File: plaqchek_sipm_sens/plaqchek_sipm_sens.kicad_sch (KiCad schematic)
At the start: 36 parts, among them J1 Conn_01x04, U14 MIC5504-1.8YM5, U16 LDK320AM-R

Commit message: finish schematic
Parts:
- removed C11, C16, C22: 0.1uF, symbol Device:C_Small
- removed C3, C37: 1nF, symbol Device:C_Small
- removed C43, C44: 1uF, symbol Device:C_Small
- removed C45, C46: 10nF, symbol Device:C_Small
- removed D1: D_SiPM, symbol Device:D_SiPM
- removed R1: 7k, symbol Device:R_Small_US
- removed R11: 10k, symbol Device:R_Small_US
- removed R12, R14: 0, symbol Device:R_Small_US
- removed R20: 22R, symbol Device:R_Small_US
- removed R35, R36: 50R, symbol Device:R_Small_US
- removed U13: ~, symbol plaqchek_mlb:MCP1501T-50E
- removed U16: LDK320AM-R, symbol plaqchek_mlb:LDK320AM-R
- removed U2, U4, U9: ~, symbol plaqchek_mlb:OPA814
- removed U5: ~, symbol plaqchek_mlb:MCP33131-10-E/MS
- added C19, C28, C29, C31, C9: 1uF, symbol Device:C_Small
- added C26: 0.33uF, symbol Device:C_Small
- added H1, H2, H3, H4: MountingHole_Pad, symbol Mechanical:MountingHole_Pad
- added J3: Conn_01x05, symbol Connector_Generic:Conn_01x05
- added R1 (x3), R15, R16, R17: 0, symbol Device:R_Small_US
- added R1 (x4): 0R, symbol Device:R_Small_US
- added R10: 350kR, symbol Device:R_Small_US
- added TP1, TP10, TP2, TP3, TP4, TP6, TP8, TP9: TestPoint, symbol Connector:TestPoint
- added TP10: -5VA, symbol Connector:TestPoint
- added TP9: 5VA, symbol Connector:TestPoint
- added U10: LDK320AM-R, symbol plaqchek_mlb:LDK320AM-R
- added U5: TPS7A2050PDBVR, symbol plaqchek:TPS7A2050PDBVR
- added U8: MC79M05_TO252, Package_TO_SOT_SMD:TO-252-2, symbol Regulator_Linear:MC79M05_TO252
- added U8: RT9072BGB, symbol plaqchek:RT9072BGB
- C10: value 0.1uF -> 1uF
- C17: value 1.7nF -> 0.18uF
- C18: value 10uF -> 1uF
- C20: value 0.1uF -> 2.2uF
- C21: value 0.1uF -> 1nF
- R13: value 10k -> 0R; now fitted
- R19: value 0 -> 100kR; now fitted
- R29: value 350kR -> 2.3kR
- R30: value 100kR -> 80kR
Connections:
- net SIPM_44V is gone; now on net SPI_3V3_ADC_CS: J1.1 (Pin_1)
- net VREF_ADC is gone; now on net SIPM_BIAS_OUT: C18.1
- net +1V8: now also R1.1, TP4.1; no longer C21.1, C38.1, U14.5 (VOUT)
- net +3V3: now also R13.2, J3.3 (Pin_3), TP9.1; no longer J1.3 (Pin_3), U14.3 (EN)
- net +5.35V: now also C29.1, R10.1, U10.5 (OUT); no longer C10.2, C20.1, R29.1
- net +6V: now also C28.1, C9.1, J3.2 (Pin_2), R17.2, U10.1 (IN), U10.3 (EN), U5.1 (IN); no longer J1.2 (Pin_2)
- net GND: now also C10.2, R19.2, C19.2, C26.1, C28.2, C29.2, C31.1, C9.2, J3.5 (Pin_5), R1.1, R1.2, R1.2, R1.2, R1.2, U10.2 (GND), U5.2 (GND), U8.1 (GND), U8.2 (SHDN); no longer C10.1, C21.2, R13.1
- net SPI_3V3_ADC_MISO: now also J1.2 (Pin_2)
- net SPI_3V3_ADC_SCLK: now also J1.3 (Pin_3)
- net at R29.2, R30.1: now also C21.2, U8.4 (FB)
- net at R19.1: now also R10.2, U10.4 (ADJ)
- net AIN_FILT renamed SIPM_BIAS_OUT
- net SIPM_BIAS_OUT: now also J3.1 (Pin_1), TP8.1, U8.1 (VIN)
- new net: C10.1, R15.2, TP9.1, U5.5 (OUT)
- new net: C19.1, C20.1, C21.1, R1.2, R29.1, TP2.1, U8.5 (VOUT)
- new net: C38.1, R1.2, TP3.1, U14.5 (VOUT)
- new net: H4.1, R1.1
- new net: C31.2, R16.2, TP10.1, U8.3 (VO)
- new net: H2.1, R1.1
- new net: H1.1, R1.1
- new net: R1.2, U8.2 (SHDN)
- new net: R17.1, U5.3 (EN)
- new net: R13.1, U14.3 (EN)
- new net: H3.1, R1.1
- new net +5VA: R15.1, TP6.1
- new net -5VA: R16.1, TP10.1
- new net -6V5: C26.2, J3.4 (Pin_4), U8.2 (VI)
- new net PD_BIAS: R1.1, TP1.1
- no-connect marks 0 -> 1
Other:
- added sheet SIPM Readout (plaqchek_sipm_read.kicad_sch)
- note added: "Max dropout V = 1.1V"
- note added: "Max dropout V = 145mV"
- note added: "R2 = R1 / (VOUT / 1.25V - 1) R1 must be below 100k Compensation capacitance = 25µs/R1"
- note removed: "Antialiasing Filter"
- note removed: "Buffer GBW = 250MHz"
- note removed: "C_in = 2.5pF, C_SiPM = 580pF, GBW = 250MHz Cf > 333 pF Choose Cf = 1nF"
- note removed: "Cf > (C_in + C_SiPM) / (Rf*GBW))"
- note removed: "Iout = 20mA"
- note removed: "Max 60Mhz"
- note removed: "Optional 2nd stage"
- note removed: "PDE = 62% at 420nm 12V Vov Gain = 7.2*10^6 Estimate 10^11 photons Thus Imax = (1.6*10^-16 C / photon) * (10^9 photons) * 0.62 * 7.2*10^6 = 0.00071424 A For Vswing = 5V: R = 2.5/0.00071424 = 7k ohms For 10^7 photons: V = 0.05V"
- note removed: "Place R14, R12 close to output of U9 R19 close to U2"
- note removed: "TIA - 1st stage"
- note removed: "Vin range: 5.2V to 5.5V Vout = 5V"
- note removed: "breakdown coltage = 32.5V typ 32V-33V Target Vov of around 12V Max Vov = 16V Min Vov = 5V Targed vbias = 44.5V max vbias = 48.5V min vbias = 37.5V"
- note removed: "cutoff freq = 2MHz"
- moved on the sheet: C36, C38, U14

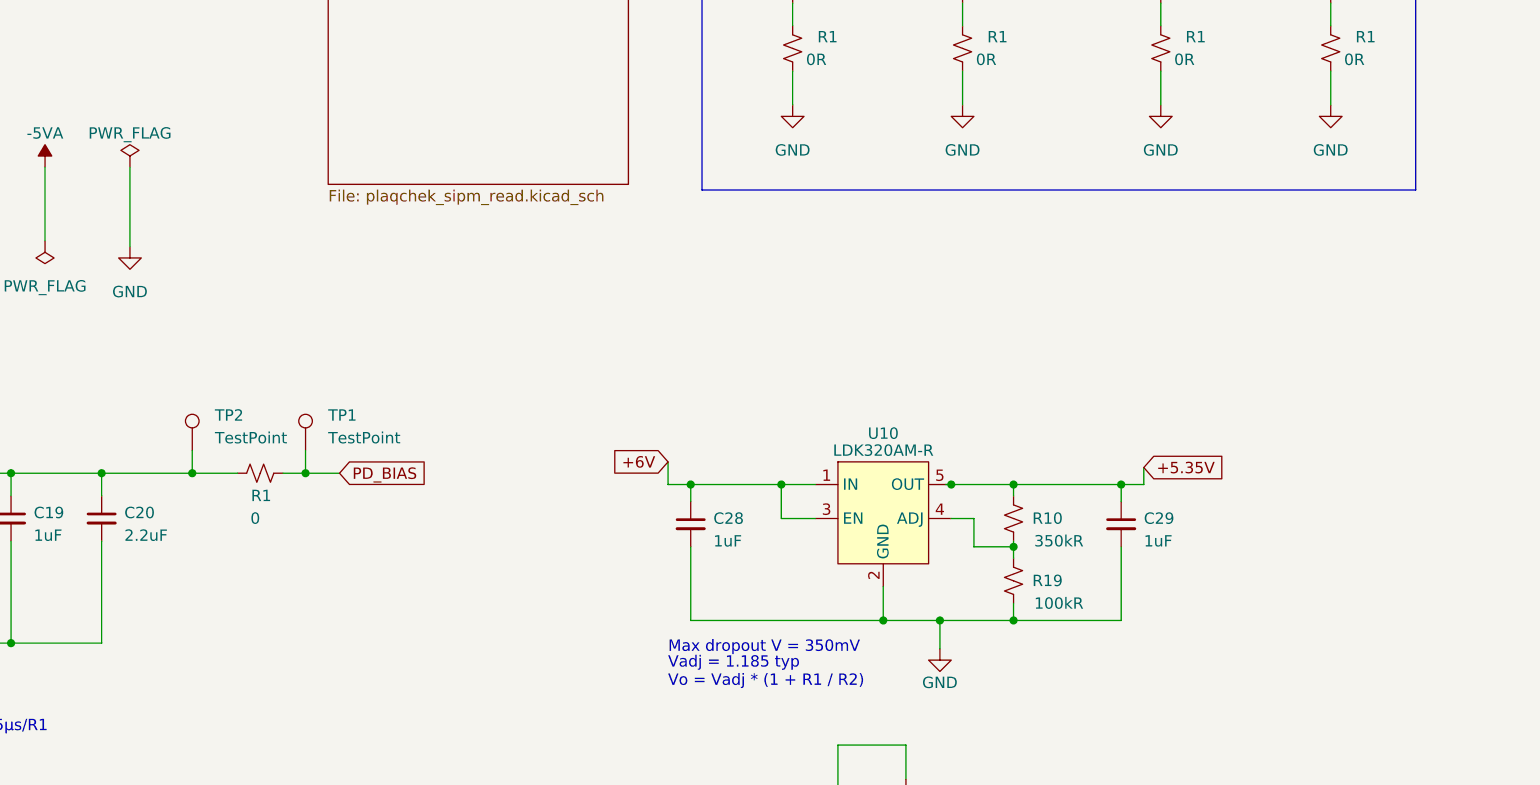
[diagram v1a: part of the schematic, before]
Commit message: modify TIA feedback cap value for new op amp, assign some footprints
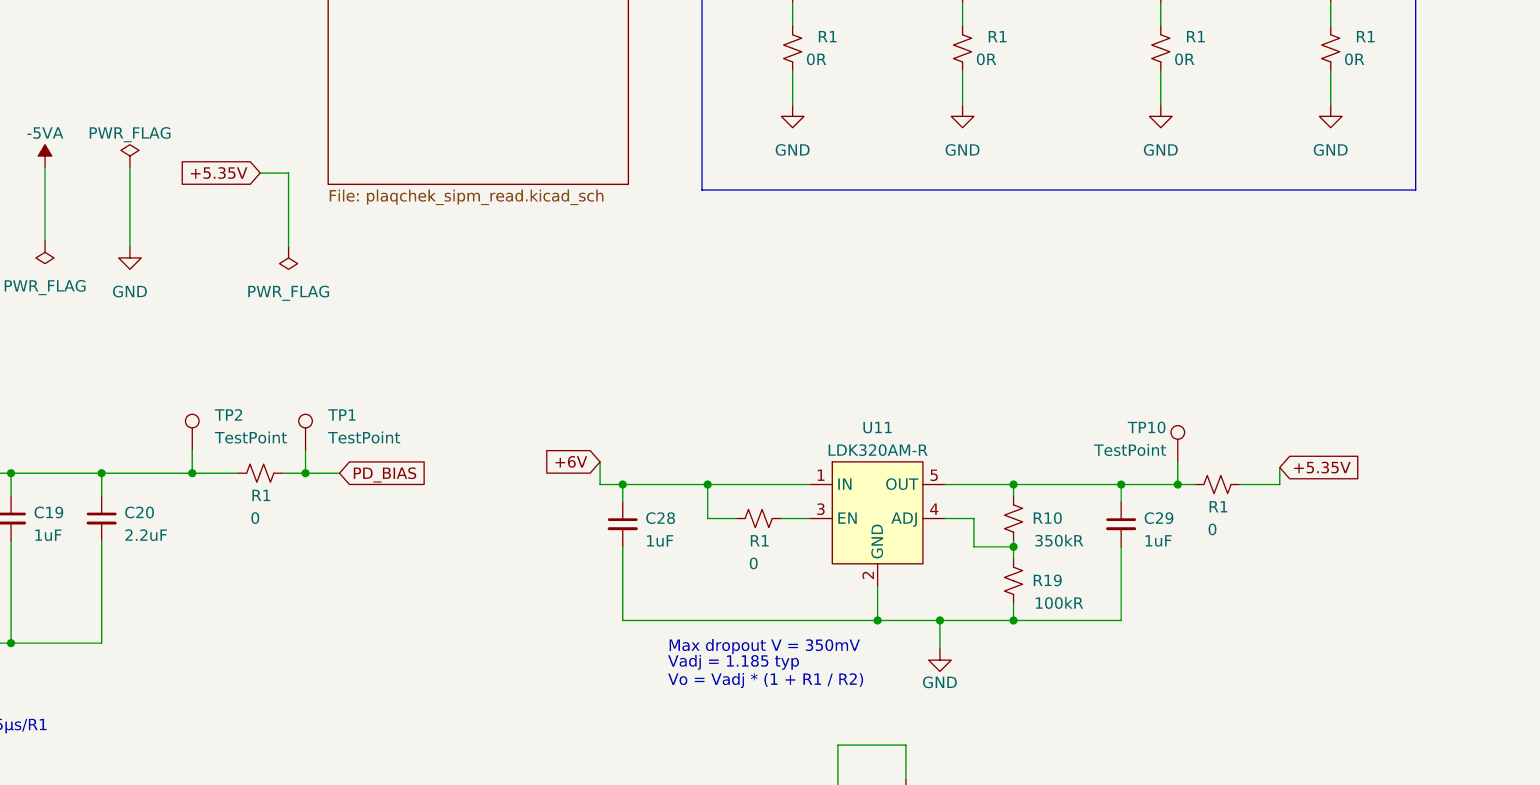
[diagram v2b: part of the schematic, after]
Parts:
- removed U10: LDK320AM-R, symbol plaqchek_mlb:LDK320AM-R
- added R1 (x2): 0, Resistor_SMD:R_0603_1608Metric_Pad0.98x0.95mm_HandSolder, symbol Device:R_Small_US
- added TP10: TestPoint, TestPoint:TestPoint_Pad_1.5x1.5mm, symbol Connector:TestPoint
- added U11: LDK320AM-R, Package_TO_SOT_SMD:SOT-23-5_HandSoldering, symbol plaqchek:LDK320AM-R
- C10, C17, C18, C19, C20, C21, C26, C28, C29, C31, C36, C38, C9: footprint (none) -> Capacitor_SMD:C_0603_1608Metric_Pad1.08x0.95mm_HandSolder
- H1, H2, H3, H4: footprint (none) -> MountingHole:MountingHole_3.2mm_M3_Pad_Via
- J1, J3, R1, R10, R13, R15, R16, R17, R19, R29, R30: footprint (none) -> Resistor_SMD:R_0603_1608Metric_Pad0.98x0.95mm_HandSolder
- TP1, TP10, TP2, TP3, TP4, TP6, TP8, TP9: footprint (none) -> TestPoint:TestPoint_Pad_1.5x1.5mm
- U14: footprint Package_TO_SOT_SMD:SOT-23-5 -> Package_TO_SOT_SMD:SOT-23-5_HandSoldering
- U5, U8: footprint (none) -> Package_TO_SOT_SMD:SOT-23-5_HandSoldering
- U8: footprint Package_TO_SOT_SMD:TO-252-2 -> Package_TO_SOT_SMD:TO-252-3_TabPin2
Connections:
- net +5.35V: now also R1.1; no longer C29.1, R10.1
- net +6V: now also R1.2, U11.1 (IN)
- net GND: now also U11.2 (GND)
- net at R10.2, R19.1: now also U11.4 (ADJ)
- new net: R1.1, U11.3 (EN)
- new net: C29.1, R1.2, R10.1, TP10.1, U11.5 (OUT)
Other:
- moved on the sheet: C28

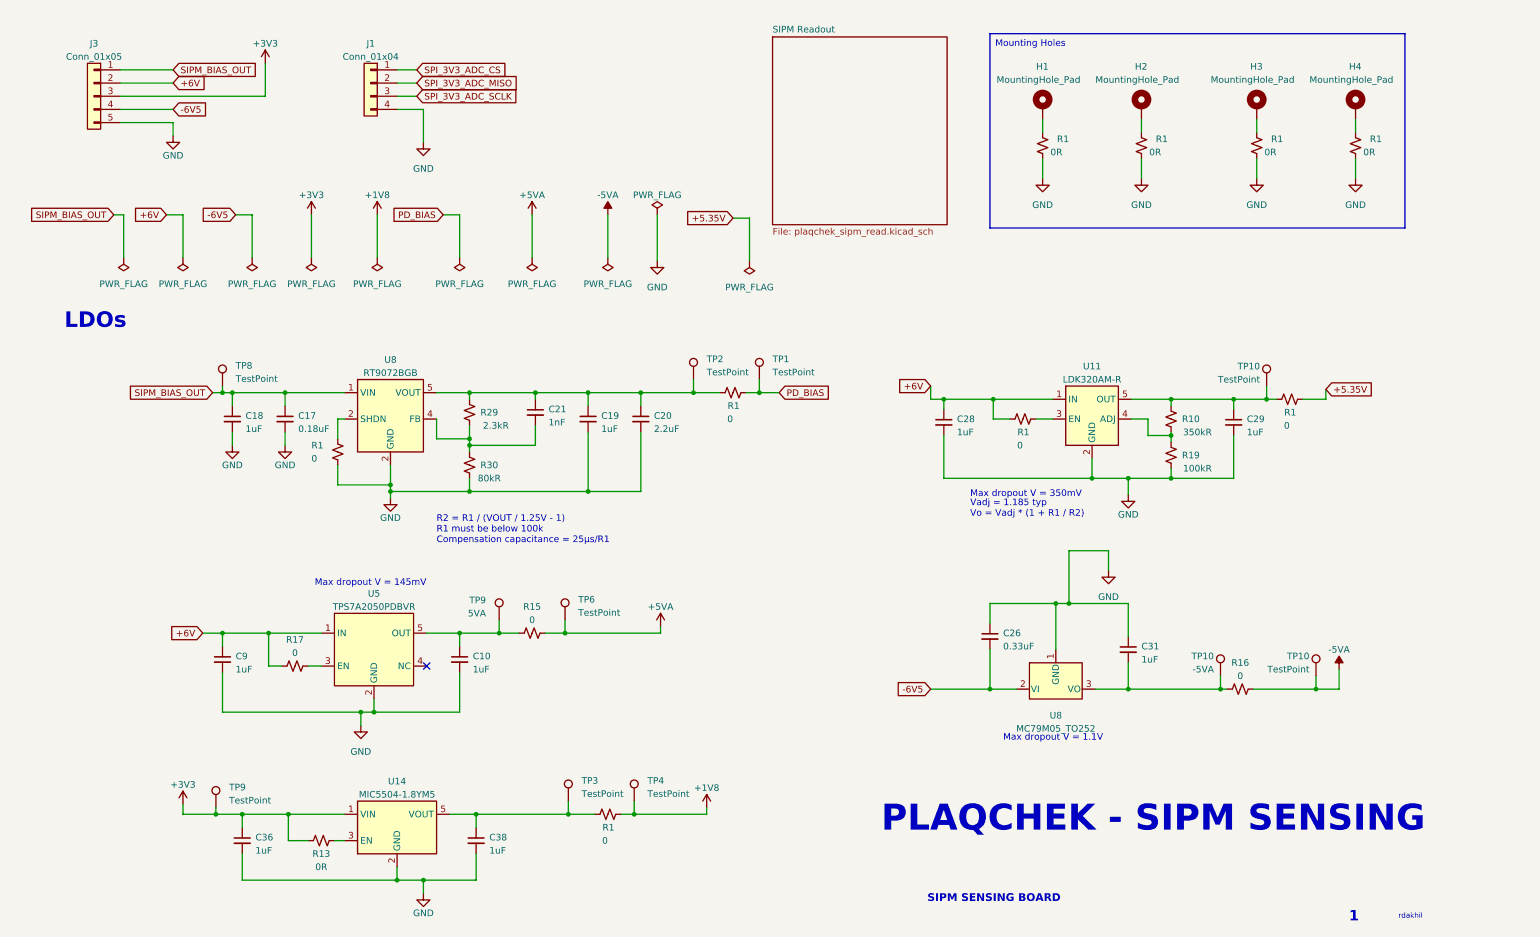
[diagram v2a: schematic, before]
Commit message: more footprints and some value fixes
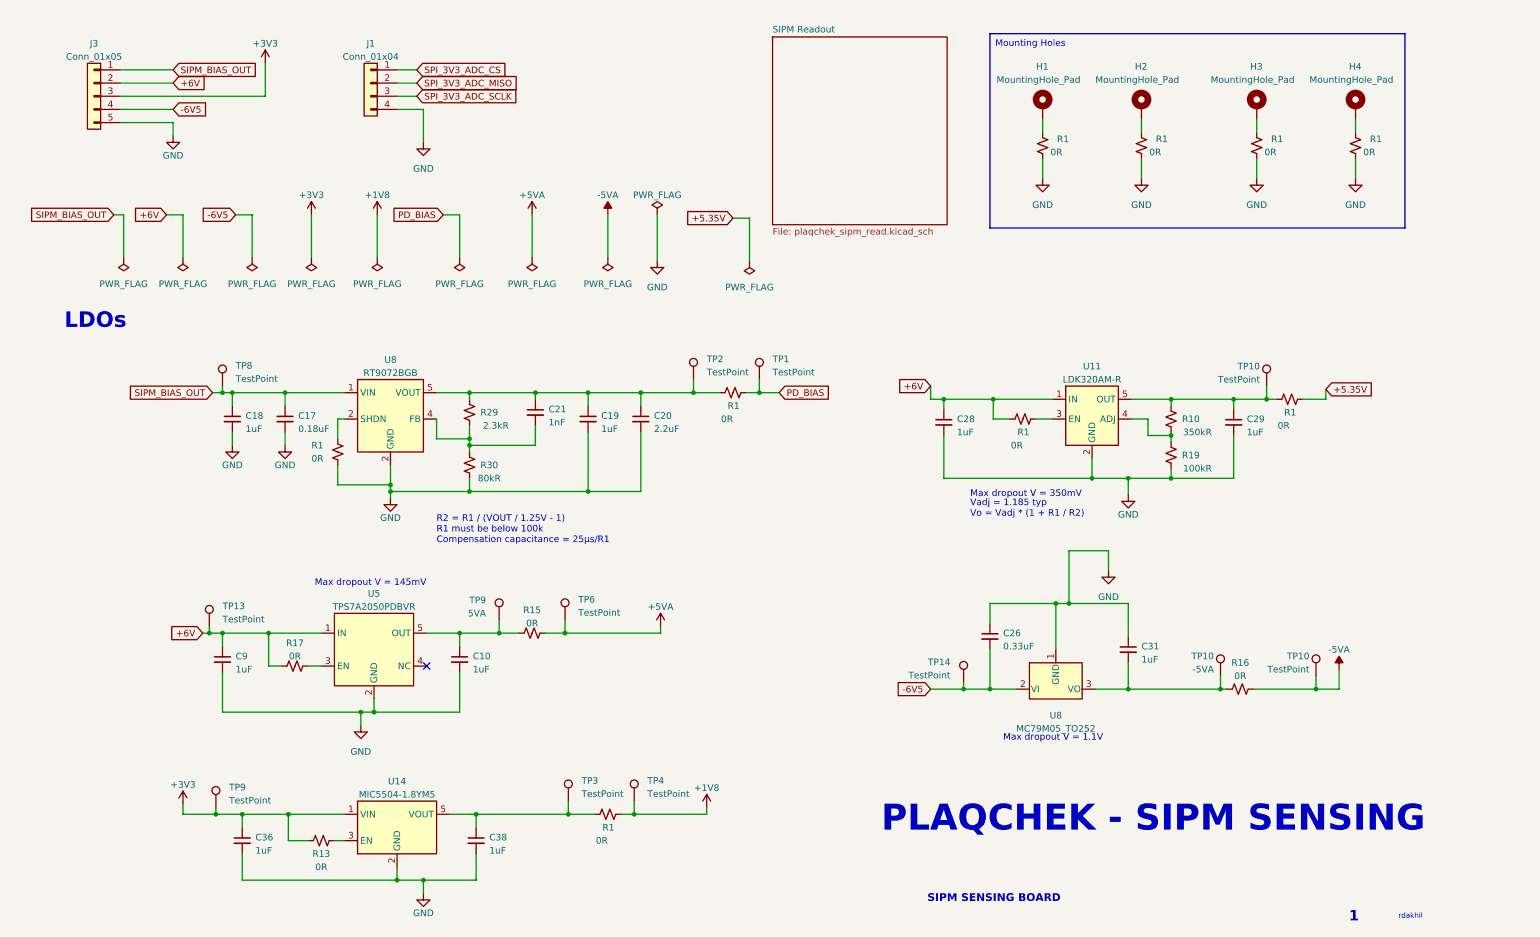
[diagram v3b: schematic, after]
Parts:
- added TP13, TP14: TestPoint, TestPoint:TestPoint_Pad_1.5x1.5mm, symbol Connector:TestPoint
- R1, R15, R16, R17: value 0 -> 0R
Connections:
- net +6V: now also TP13.1
- net -6V5: now also TP14.1
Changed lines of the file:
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@@
   (junction (at 98.425 100.33) (diameter 0) (color 0 0 0 0)
   )
+  (junction (at 48.26 137.795) (diameter 0) (color 0 0 0 0)
+  )
   (junction (at 99.695 172.72) (diameter 0) (color 0 0 0 0)
   )
@@
   (junction (at 198.755 148.59) (diameter 0) (color 0 0 0 0)
   )
+  (junction (at 193.675 148.59) (diameter 0) (color 0 0 0 0)
+  )
   (junction (at 243.205 148.59) (diameter 0) (color 0 0 0 0)
   )
@@
     (stroke (width 0) (type default))
   )
-  (wire (pts (xy 50.8 137.795) (xy 46.99 137.795))
+  (wire (pts (xy 50.8 137.795) (xy 48.26 137.795))
     (stroke (width 0) (type default))
   )
@@
     (stroke (width 0) (type default))
   )
+  (wire (pts (xy 48.26 137.795) (xy 46.99 137.795))
+    (stroke (width 0) (type default))
+  )
   (wire (pts (xy 56.515 57.15) (xy 56.515 65.405))
     (stroke (width 0) (type default))
@@
     (stroke (width 0) (type default))
   )
+  (wire (pts (xy 193.675 148.59) (xy 198.755 148.59))
+    (stroke (width 0) (type default))
+  )
   (wire (pts (xy 59.69 144.145) (xy 59.69 137.795))
     (stroke (width 0) (type default))
@@
     (stroke (width 0) (type default))
   )
+  (wire (pts (xy 48.26 136.525) (xy 48.26 137.795))
+    (stroke (width 0) (type default))
+  )
+  (wire (pts (xy 193.675 147.32) (xy 193.675 148.59))
+    (stroke (width 0) (type default))
+  )
   (wire (pts (xy 226.06 92.71) (xy 233.68 92.71))
     (stroke (width 0) (type default))
@@
     (stroke (width 0) (type default))
   )
-  (wire (pts (xy 187.325 148.59) (xy 198.755 148.59))
+  (wire (pts (xy 187.325 148.59) (xy 193.675 148.59))
     (stroke (width 0) (type default))
   )
@@
       (effects (font (size 1.27 1.27)) (justify right))
     )
-    (property "Value" "0" (at 205.105 101.6 90)
+    (property "Value" "0R" (at 205.105 101.6 90)
       (effects (font (size 1.27 1.27)) (justify right))
     )
@@
       (effects (font (size 1.27 1.27)) (justify right))
     )
-    (property "Value" "0" (at 125.095 177.8 90)
+    (property "Value" "0R" (at 125.095 177.8 90)
       (effects (font (size 1.27 1.27)) (justify right))
     )
@@
       (effects (font (size 1.27 1.27)))
     )
-    (property "Value" "0" (at 247.015 146.05 90)
+    (property "Value" "0R" (at 247.015 146.05 90)
       (effects (font (size 1.27 1.27)))
     )
@@
       (effects (font (size 1.27 1.27)) (justify right))
     )
-    (property "Value" "0" (at 67.945 104.14 0)
+    (property "Value" "0R" (at 67.945 104.14 0)
       (effects (font (size 1.27 1.27)) (justify right))
     )
@@
   (symbol (lib_id "Device:R_Small_US") (at 64.77 144.145 270) (unit 1)
     (in_bom yes) (on_board yes) (dnp no) (fields_autoplaced)
-    (property "Reference" "R17" (at 64.77 139.065 90)
+    (property "Reference" "R17" (at 64.77 139.7 90)
       (effects (font (size 1.27 1.27)))
     )
-    (property "Value" "0" (at 64.77 141.605 90)
+    (property "Value" "0R" (at 64.77 142.24 90)
       (effects (font (size 1.27 1.27)))
     )
@@
   (symbol (lib_id "Device:R_Small_US") (at 110.49 137.795 270) (unit 1)
     (in_bom yes) (on_board yes) (dnp no) (fields_autoplaced)
-    (property "Reference" "R15" (at 110.49 132.715 90)
+    (property "Reference" "R15" (at 110.49 133.35 90)
       (effects (font (size 1.27 1.27)))
     )
-    (property "Value" "0" (at 110.49 135.255 90)
+    (property "Value" "0R" (at 110.49 135.89 90)
       (effects (font (size 1.27 1.27)))
     )
@@
     )
   )
+  (symbol (lib_id "Connector:TestPoint") (at 193.675 147.32 0) (mirror y) (unit 1)
+    (in_bom yes) (on_board yes) (dnp no) (fields_autoplaced)
+    (property "Reference" "TP14" (at 191.135 143.383 0)
+      (effects (font (size 1.27 1.27)) (justify left))
+    )
+    (property "Value" "TestPoint" (at 191.135 145.923 0)
+      (effects (font (size 1.27 1.27)) (justify left))
+    )
+    (property "Footprint" "TestPoint:TestPoint_Pad_1.5x1.5mm" (at 188.595 147.32 0)
+      (effects (font (size 1.27 1.27)) hide)
+    )
+    (property "Datasheet" "~" (at 188.595 147.32 0)
+      (effects (font (size 1.27 1.27)) hide)
+    )
+    (pin "1")
+    (instances
+      (project "plaqchek_sipm_sens"
+        (path "/ae49fc30-e8ec-4ce4-a893-3d974076e2da"
+          (reference "TP14") (unit 1)
+        )
+      )
+    )
+  )
   (symbol (lib_id "Connector:TestPoint") (at 243.205 146.05 0) (mirror y) (unit 1)
     (in_bom yes) (on_board yes) (dnp no)
@@
       (effects (font (size 1.27 1.27)) (justify right))
     )
-    (property "Value" "0" (at 149.225 96.52 90)
+    (property "Value" "0R" (at 149.225 96.52 90)
       (effects (font (size 1.27 1.27)) (justify right))
     )
@@
       (effects (font (size 1.27 1.27)) (justify right))
     )
-    (property "Value" "0" (at 256.54 97.79 90)
+    (property "Value" "0R" (at 256.54 97.79 90)
       (effects (font (size 1.27 1.27)) (justify right))
     )
@@
         )
       )
+    )
+  )
+  (symbol (lib_id "Connector:TestPoint") (at 48.26 136.525 0) (unit 1)
+    (in_bom yes) (on_board yes) (dnp no) (fields_autoplaced)
+    (property "Reference" "TP13" (at 50.8 132.588 0)
+      (effects (font (size 1.27 1.27)) (justify left))
+    )
+    (property "Value" "TestPoint" (at 50.8 135.128 0)
+      (effects (font (size 1.27 1.27)) (justify left))
+    )
+    (property "Footprint" "TestPoint:TestPoint_Pad_1.5x1.5mm" (at 53.34 136.525 0)
+      (effects (font (size 1.27 1.27)) hide)
+    )
+    (property "Datasheet" "~" (at 53.34 136.525 0)
+      (effects (font (size 1.27 1.27)) hide)
+    )
+    (pin "1")
+    (instances
+      (project "plaqchek_sipm_sens"
+        (path "/ae49fc30-e8ec-4ce4-a893-3d974076e2da"
+          (reference "TP13") (unit 1)
+        )
+      )
